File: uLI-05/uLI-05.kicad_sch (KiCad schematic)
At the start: 50 parts, among them J1 C, J2 USB_B, J3 RJ25, J4 RJ25, J5 PROG, Q1 IRF7306, U1 LM78M05_TO252, U2 PC817, U3 PC817, U4 PIC18F14K50-EP, U5 ADM2483xRW, U6 USBLC6-2SC6, Y1 12MHz

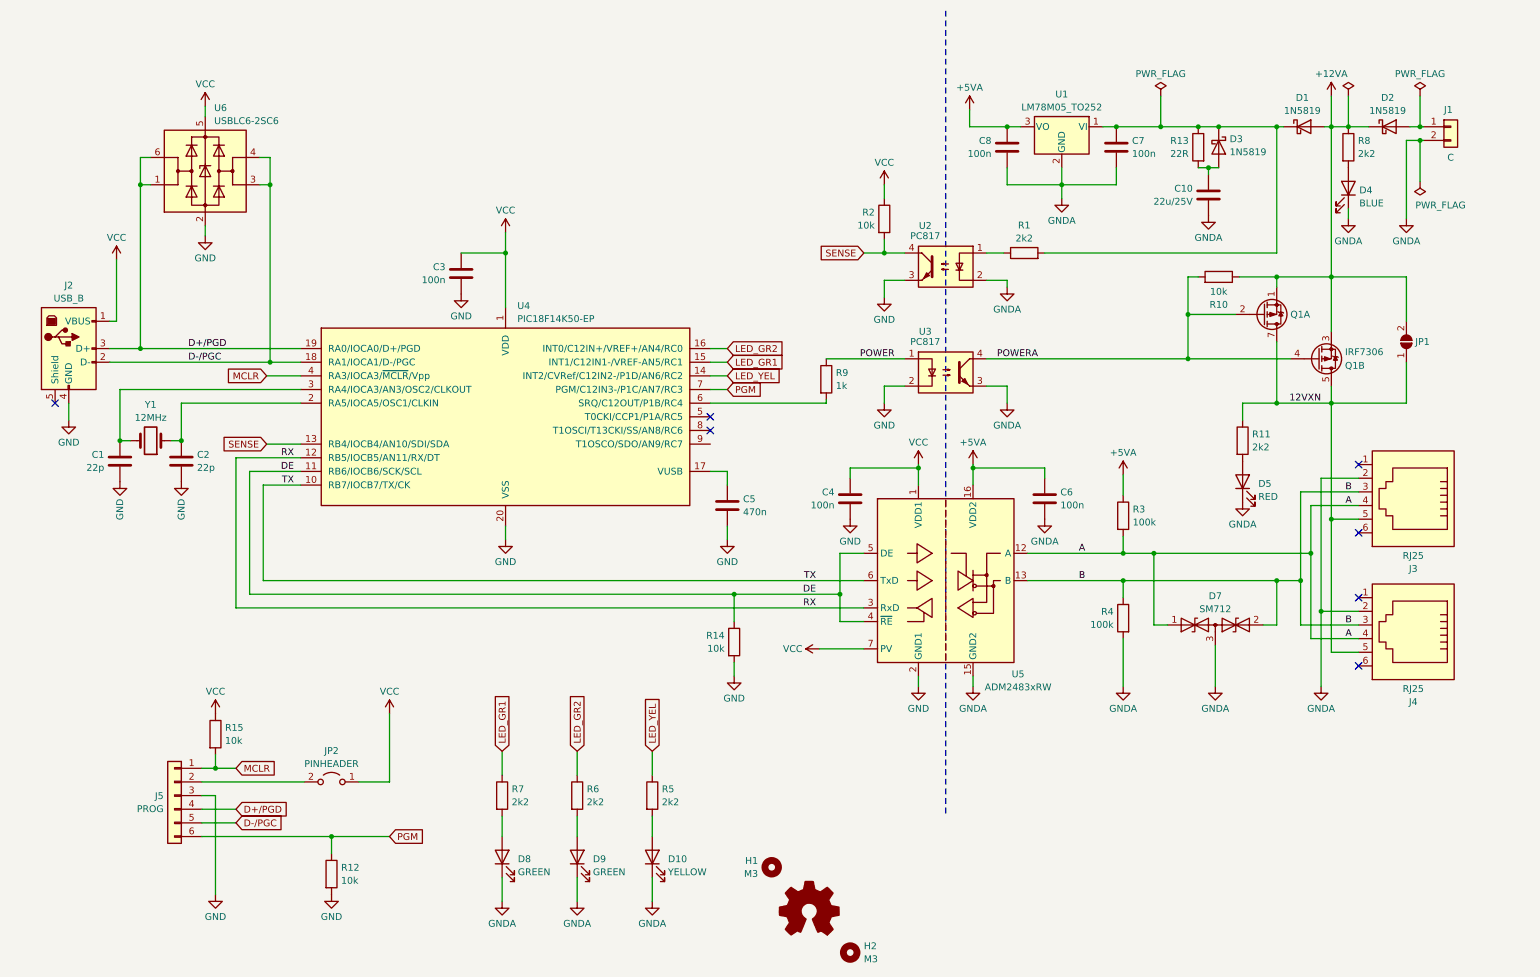
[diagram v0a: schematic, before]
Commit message: Add R16 distinguish resistor.
To distinguish between uLI-4 & uLI-5 in firmware.
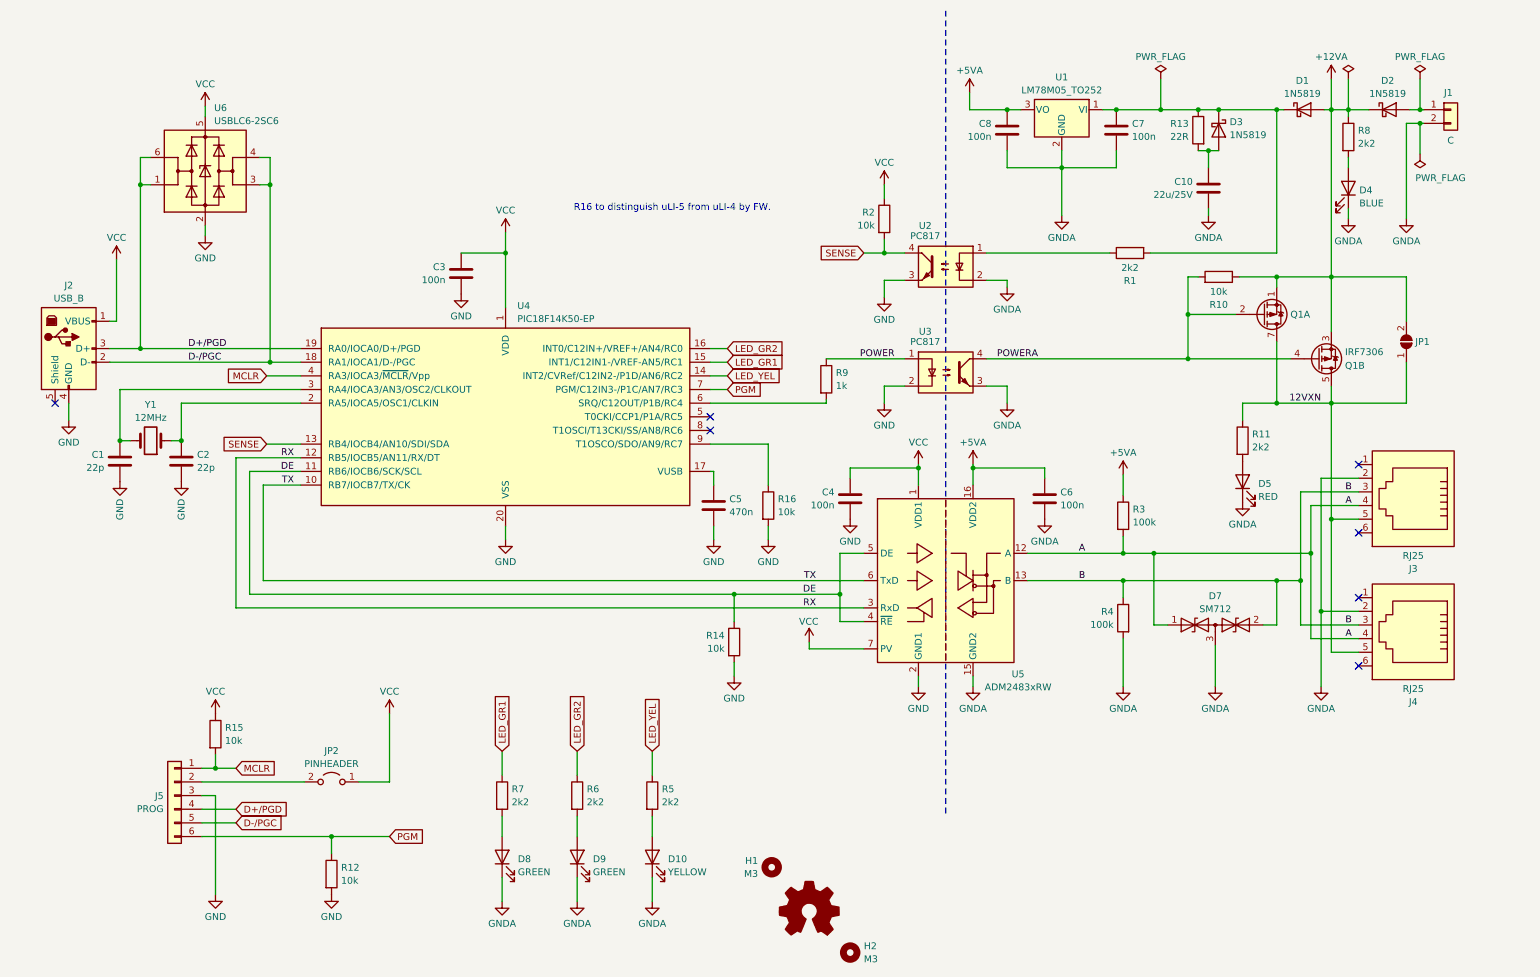
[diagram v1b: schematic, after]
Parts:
- added R16: 10k, symbol Device:R
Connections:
- net GND: now also R16.2
- net at U4.9 (T1OSCO/SDO/AN9/RC7): now also R16.1
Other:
- note added: "R16 to distinguish uLI-5 from uLI-4 by FW."
- moved on the sheet: C10, C5, C7, C8, D1, D2, D3, J1, R1, R13, R8, U1

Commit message: pcb: place connectors & LEDs.
Place on same positions as in uLI-4.
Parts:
- Y1: footprint Crystal:Crystal_HC49-U_Vertical -> Crystal:Crystal_HC49-4H_Vertical
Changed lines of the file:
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@@
       (effects (font (size 1.27 1.27)))
     )
-    (property "Footprint" "Crystal:Crystal_HC49-U_Vertical" (at 38.735 93.98 0)
+    (property "Footprint" "Crystal:Crystal_HC49-4H_Vertical" (at 38.735 93.98 0)
       (effects (font (size 1.27 1.27)) hide)
     )

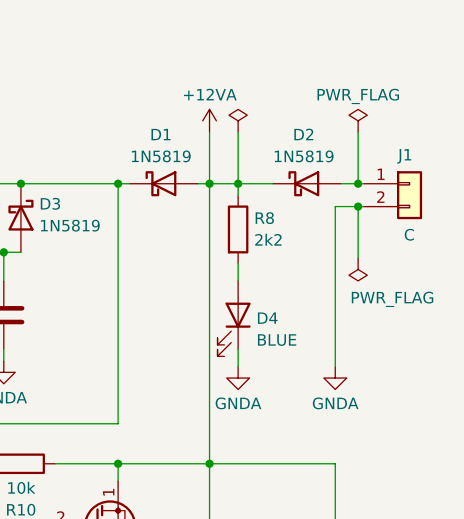
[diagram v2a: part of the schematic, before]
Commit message: Add STL1550 power connector.
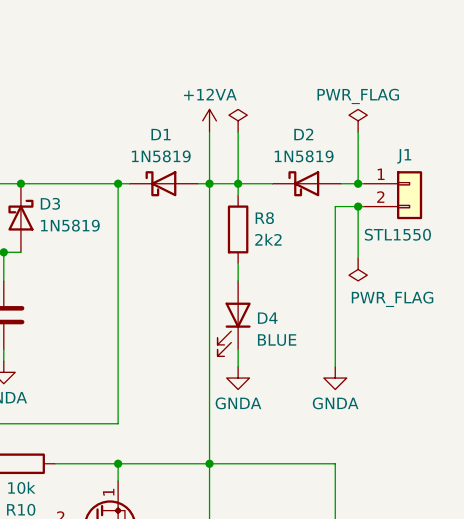
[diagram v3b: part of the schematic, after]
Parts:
- J1: value C -> STL1550; footprint (none) -> Connector_Phoenix_MC:PhoenixContact_MC_1,5_2-G-3.5_1x02_P3.50mm_Horizontal
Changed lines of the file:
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@@
       (effects (font (size 1.27 1.27)) (justify left))
     )
-    (property "Value" "C" (at 280.035 38.1 0)
+    (property "Value" "STL1550" (at 275.59 38.1 0)
       (effects (font (size 1.27 1.27)) (justify left))
     )
-    (property "Footprint" "" (at 280.67 32.385 0)
+    (property "Footprint" "Connector_Phoenix_MC:PhoenixContact_MC_1,5_2-G-3.5_1x02_P3.50mm_Horizontal" (at 280.67 32.385 0)
       (effects (font (size 1.27 1.27)) hide)
     )

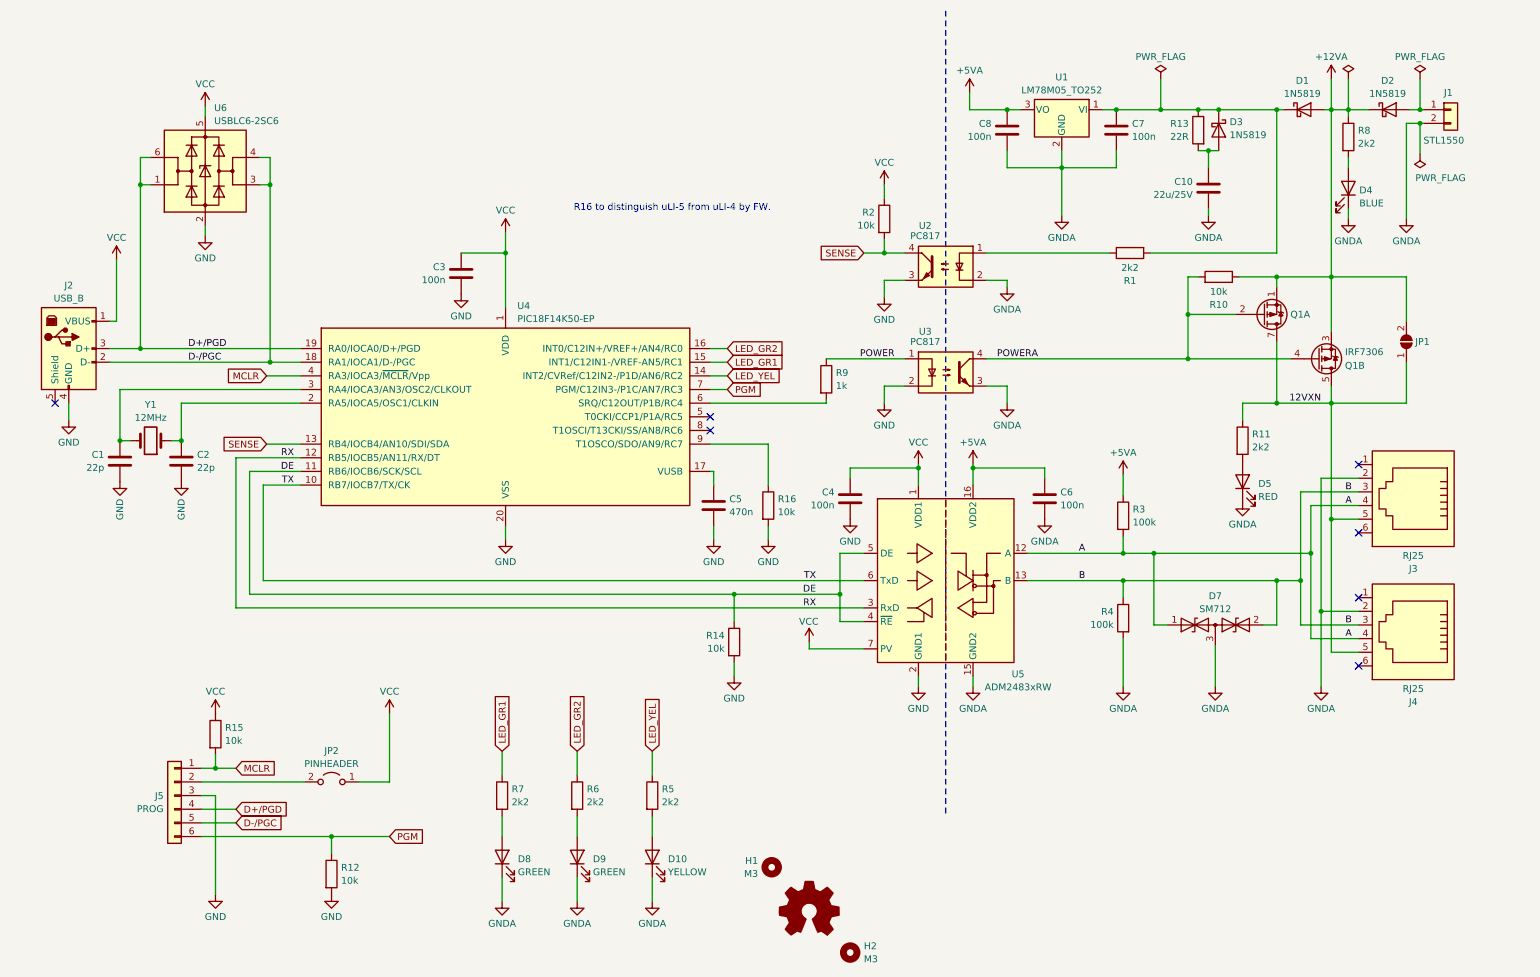
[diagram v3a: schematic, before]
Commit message: pcb: wire USB part.
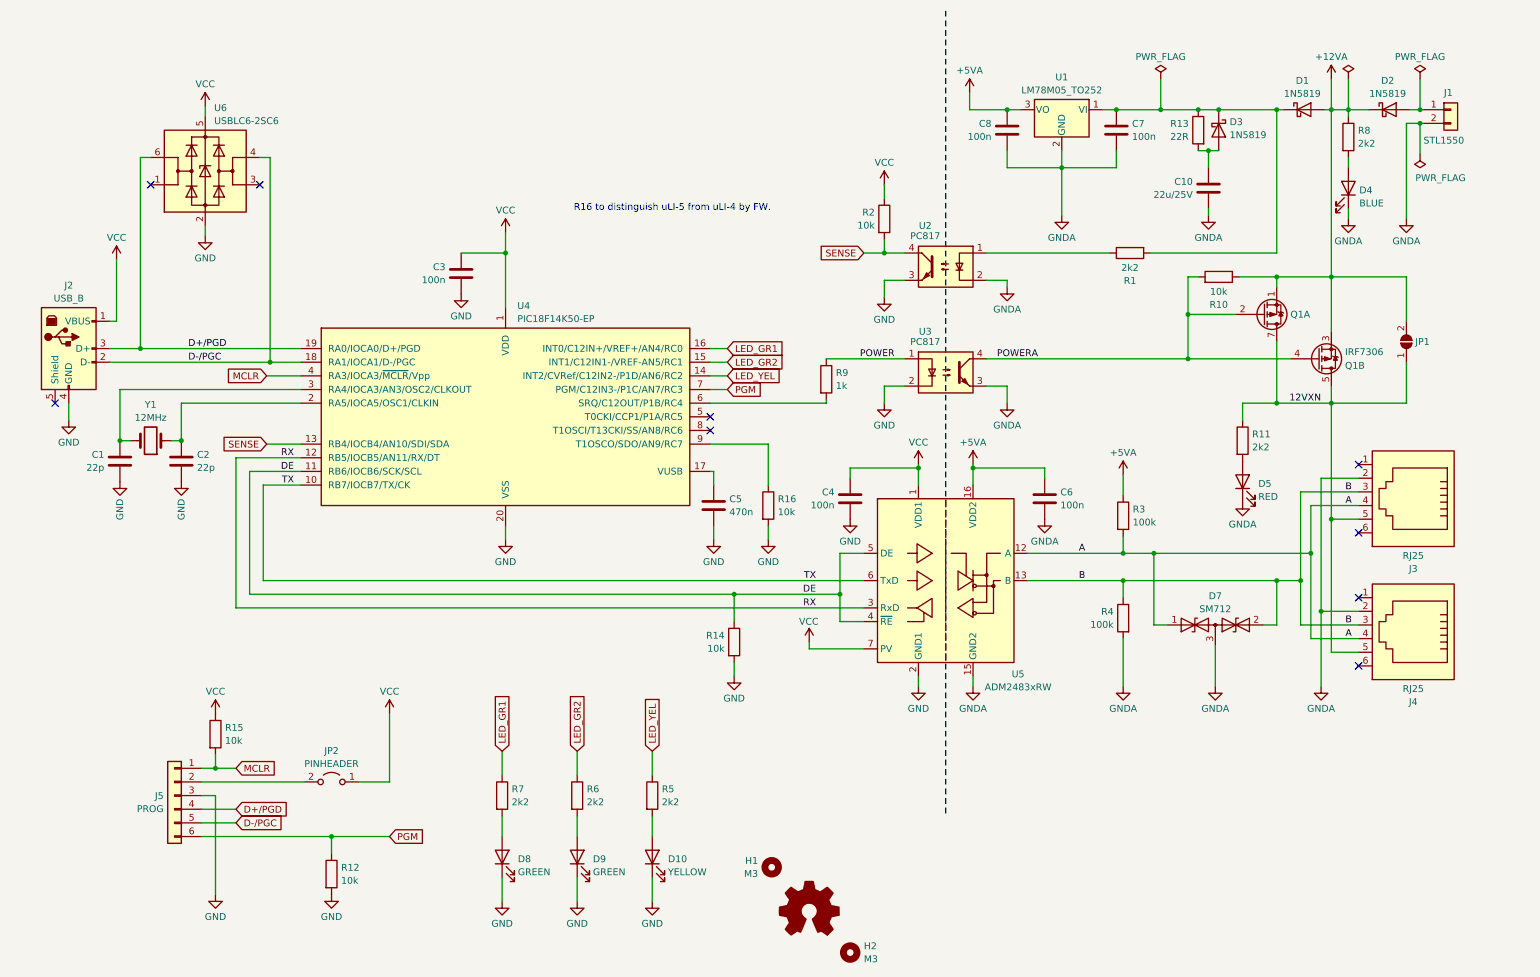
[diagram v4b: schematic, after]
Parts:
- R16: footprint (none) -> Resistor_SMD:R_0805_2012Metric
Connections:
- net D+/PGD: no longer U6.1 (I/O1)
- net D-/PGC: no longer U6.3 (I/O2)
- net GND: now also D10.1 (K), D8.1 (K), D9.1 (K)
- net GNDA: no longer D10.1 (K), D8.1 (K), D9.1 (K)
- net LED_GR1: now also U4.16 (INT0/C12IN+/VREF+/AN4/RC0); no longer U4.15 (INT1/C12IN1-/VREF-AN5/RC1)
- net LED_GR2: now also U4.15 (INT1/C12IN1-/VREF-AN5/RC1); no longer U4.16 (INT0/C12IN+/VREF+/AN4/RC0)
- no-connect marks 7 -> 9
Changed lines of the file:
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@@
   (junction (at 252.73 120.015) (diameter 0) (color 0 0 0 0)
   )
-  (junction (at 36.83 46.355) (diameter 0) (color 0 0 0 0)
-  )
   (junction (at 258.445 32.385) (diameter 0) (color 0 0 0 0)
   )
@@
   (junction (at 104.775 59.055) (diameter 0) (color 0 0 0 0)
   )
-  (junction (at 60.96 46.355) (diameter 0) (color 0 0 0 0)
-  )
   (junction (at 208.28 43.18) (diameter 0) (color 0 0 0 0)
   )
@@
   )
   (no_connect (at 263.525 111.125))
+  (no_connect (at 59.055 46.355))
   (no_connect (at 20.955 86.995))
   (no_connect (at 142.875 89.535))
@@
   (no_connect (at 263.525 123.19))
   (no_connect (at 142.875 92.075))
+  (no_connect (at 38.735 46.355))
   (no_connect (at 263.525 135.89))
   (wire (pts (xy 235.585 40.005) (xy 237.49 40.005))
@@
     (stroke (width 0) (type default))
   )
-  (wire (pts (xy 36.83 46.355) (xy 36.83 76.835))
+  (wire (pts (xy 36.83 41.275) (xy 36.83 76.835))
     (stroke (width 0) (type default))
   )
@@
     (stroke (width 0) (type default))
   )
-  (wire (pts (xy 59.055 46.355) (xy 60.96 46.355))
-    (stroke (width 0) (type default))
-  )
-  (wire (pts (xy 60.96 41.275) (xy 60.96 46.355))
-    (stroke (width 0) (type default))
-  )
   (wire (pts (xy 252.73 120.015) (xy 252.73 128.27))
     (stroke (width 0) (type default))
@@
     (stroke (width 0) (type default))
   )
-  (wire (pts (xy 36.83 41.275) (xy 36.83 46.355))
-    (stroke (width 0) (type default))
-  )
   (wire (pts (xy 83.185 157.48) (xy 77.47 157.48))
     (stroke (width 0) (type default))
@@
     (stroke (width 0) (type default))
   )
-  (wire (pts (xy 36.83 46.355) (xy 38.735 46.355))
-    (stroke (width 0) (type default))
-  )
   (wire (pts (xy 104.14 179.705) (xy 104.14 175.26))
     (stroke (width 0) (type default))
@@
     (stroke (width 0) (type default))
   )
-  (wire (pts (xy 60.96 46.355) (xy 60.96 79.375))
+  (wire (pts (xy 60.96 41.275) (xy 60.96 79.375))
     (stroke (width 0) (type default))
   )
@@
     (effects (font (size 1.27 1.27)) (justify right bottom))
   )
-  (global_label "LED_GR2" (shape input) (at 146.05 76.835 0) (fields_autoplaced)
+  (global_label "LED_GR2" (shape input) (at 146.05 79.375 0) (fields_autoplaced)
     (effects (font (size 1.27 1.27)) (justify left))
-    (property "Intersheetrefs" "${INTERSHEET_REFS}" (at 157.1994 76.835 0)
+    (property "Intersheetrefs" "${INTERSHEET_REFS}" (at 157.1994 79.375 0)
       (effects (font (size 1.27 1.27)) (justify left) hide)
     )
@@
     )
   )
-  (global_label "LED_GR1" (shape input) (at 146.05 79.375 0) (fields_autoplaced)
+  (global_label "LED_GR1" (shape input) (at 146.05 76.835 0) (fields_autoplaced)
     (effects (font (size 1.27 1.27)) (justify left))
-    (property "Intersheetrefs" "${INTERSHEET_REFS}" (at 157.1994 79.375 0)
+    (property "Intersheetrefs" "${INTERSHEET_REFS}" (at 157.1994 76.835 0)
       (effects (font (size 1.27 1.27)) (justify left) hide)
     )
@@
     )
   )
+  (symbol (lib_id "power:GND") (at 118.11 179.705 0) (mirror y) (unit 1)
+    (in_bom yes) (on_board yes) (dnp no) (fields_autoplaced)
+    (property "Reference" "#PWR039" (at 118.11 186.055 0)
+      (effects (font (size 1.27 1.27)) hide)
+    )
+    (property "Value" "GND" (at 118.11 183.8381 0)
+      (effects (font (size 1.27 1.27)))
+    )
+    (property "Footprint" "" (at 118.11 179.705 0)
+      (effects (font (size 1.27 1.27)) hide)
+    )
+    (property "Datasheet" "" (at 118.11 179.705 0)
+      (effects (font (size 1.27 1.27)) hide)
+    )
+    (pin "1")
+    (instances
+      (project "uLI-05"
+        (path "/78ef7769-d6f1-48f5-a16b-8d45b14bfe28"
+          (reference "#PWR039") (unit 1)
+        )
+      )
+    )
+  )
   (symbol (lib_id "power:VCC") (at 175.26 46.355 0) (unit 1)
     (in_bom yes) (on_board yes) (dnp no) (fields_autoplaced)
@@
     )
   )
-  (symbol (lib_id "power:GNDA") (at 104.14 179.705 0) (unit 1)
-    (in_bom yes) (on_board yes) (dnp no) (fields_autoplaced)
-    (property "Reference" "#PWR038" (at 104.14 186.055 0)
-      (effects (font (size 1.27 1.27)) hide)
-    )
-    (property "Value" "GNDA" (at 104.14 183.8381 0)
-      (effects (font (size 1.27 1.27)))
-    )
-    (property "Footprint" "" (at 104.14 179.705 0)
-      (effects (font (size 1.27 1.27)) hide)
-    )
-    (property "Datasheet" "" (at 104.14 179.705 0)
-      (effects (font (size 1.27 1.27)) hide)
-    )
-    (pin "1")
-    (instances
-      (project "uLI-05"
-        (path "/78ef7769-d6f1-48f5-a16b-8d45b14bfe28"
-          (reference "#PWR038") (unit 1)
-        )
-      )
-    )
-  )
   (symbol (lib_id "power:GND") (at 50.8 178.435 0) (mirror y) (unit 1)
     (in_bom yes) (on_board yes) (dnp no) (fields_autoplaced)
@@
     )
   )
-  (symbol (lib_id "power:GNDA") (at 118.11 179.705 0) (unit 1)
+  (symbol (lib_id "power:GND") (at 132.08 179.705 0) (mirror y) (unit 1)
     (in_bom yes) (on_board yes) (dnp no) (fields_autoplaced)
-    (property "Reference" "#PWR039" (at 118.11 186.055 0)
+    (property "Reference" "#PWR040" (at 132.08 186.055 0)
       (effects (font (size 1.27 1.27)) hide)
     )
-    (property "Value" "GNDA" (at 118.11 183.8381 0)
+    (property "Value" "GND" (at 132.08 183.8381 0)
       (effects (font (size 1.27 1.27)))
     )
-    (property "Footprint" "" (at 118.11 179.705 0)
+    (property "Footprint" "" (at 132.08 179.705 0)
       (effects (font (size 1.27 1.27)) hide)
     )
-    (property "Datasheet" "" (at 118.11 179.705 0)
+    (property "Datasheet" "" (at 132.08 179.705 0)
       (effects (font (size 1.27 1.27)) hide)
     )
@@
       (project "uLI-05"
         (path "/78ef7769-d6f1-48f5-a16b-8d45b14bfe28"
-          (reference "#PWR039") (unit 1)
+          (reference "#PWR040") (unit 1)
         )
       )
@@
       (effects (font (size 1.27 1.27)) (justify left))
     )
-    (property "Footprint" "" (at 151.892 106.045 90)
+    (property "Footprint" "Resistor_SMD:R_0805_2012Metric" (at 151.892 106.045 90)
       (effects (font (size 1.27 1.27)) hide)
     )
@@
     )
   )
-  (symbol (lib_id "power:GNDA") (at 132.08 179.705 0) (unit 1)
-    (in_bom yes) (on_board yes) (dnp no) (fields_autoplaced)
-    (property "Reference" "#PWR040" (at 132.08 186.055 0)
-      (effects (font (size 1.27 1.27)) hide)
-    )
-    (property "Value" "GNDA" (at 132.08 183.8381 0)
-      (effects (font (size 1.27 1.27)))
-    )
-    (property "Footprint" "" (at 132.08 179.705 0)
-      (effects (font (size 1.27 1.27)) hide)
-    )
-    (property "Datasheet" "" (at 132.08 179.705 0)
-      (effects (font (size 1.27 1.27)) hide)
-    )
-    (pin "1")
-    (instances
-      (project "uLI-05"
-        (path "/78ef7769-d6f1-48f5-a16b-8d45b14bfe28"
-          (reference "#PWR040") (unit 1)
-        )
-      )
-    )
-  )
   (symbol (lib_id "Device:R") (at 72.39 174.625 0) (unit 1)
     (in_bom yes) (on_board yes) (dnp no)
@@
         )
       )
+    )
+  )
+  (symbol (lib_id "power:GND") (at 104.14 179.705 0) (mirror y) (unit 1)
+    (in_bom yes) (on_board yes) (dnp no) (fields_autoplaced)
+    (property "Reference" "#PWR038" (at 104.14 186.055 0)
+      (effects (font (size 1.27 1.27)) hide)
+    )
+    (property "Value" "GND" (at 104.14 183.8381 0)
+      (effects (font (size 1.27 1.27)))
+    )
+    (property "Footprint" "" (at 104.14 179.705 0)
+      (effects (font (size 1.27 1.27)) hide)
+    )
+    (property "Datasheet" "" (at 104.14 179.705 0)
+      (effects (font (size 1.27 1.27)) hide)
+    )
+    (pin "1")
+    (instances
+      (project "uLI-05"
+        (path "/78ef7769-d6f1-48f5-a16b-8d45b14bfe28"
+          (reference "#PWR038") (unit 1)
+        )
+      )
